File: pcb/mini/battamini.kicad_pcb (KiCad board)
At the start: 2 copper layers, 128.3 x 99.3 mm, 38 parts

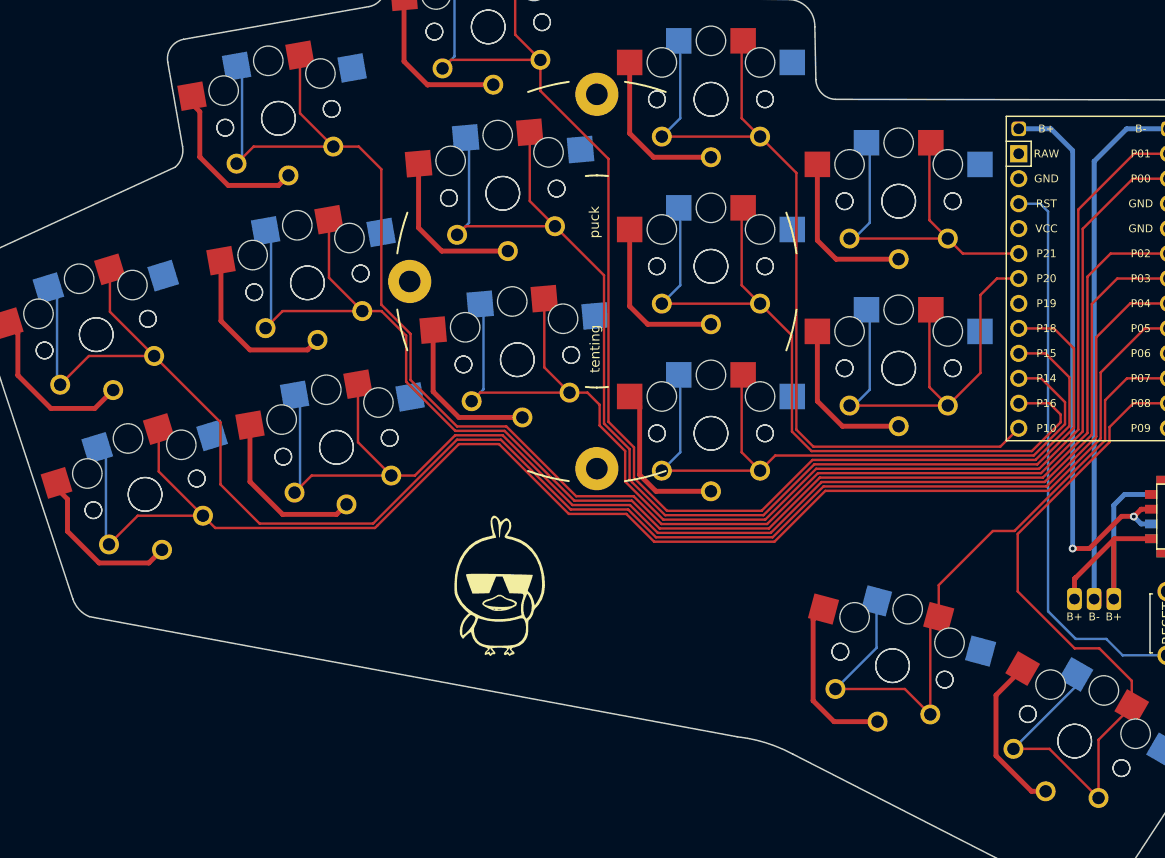
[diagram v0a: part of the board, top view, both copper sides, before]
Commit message: mini routing modification
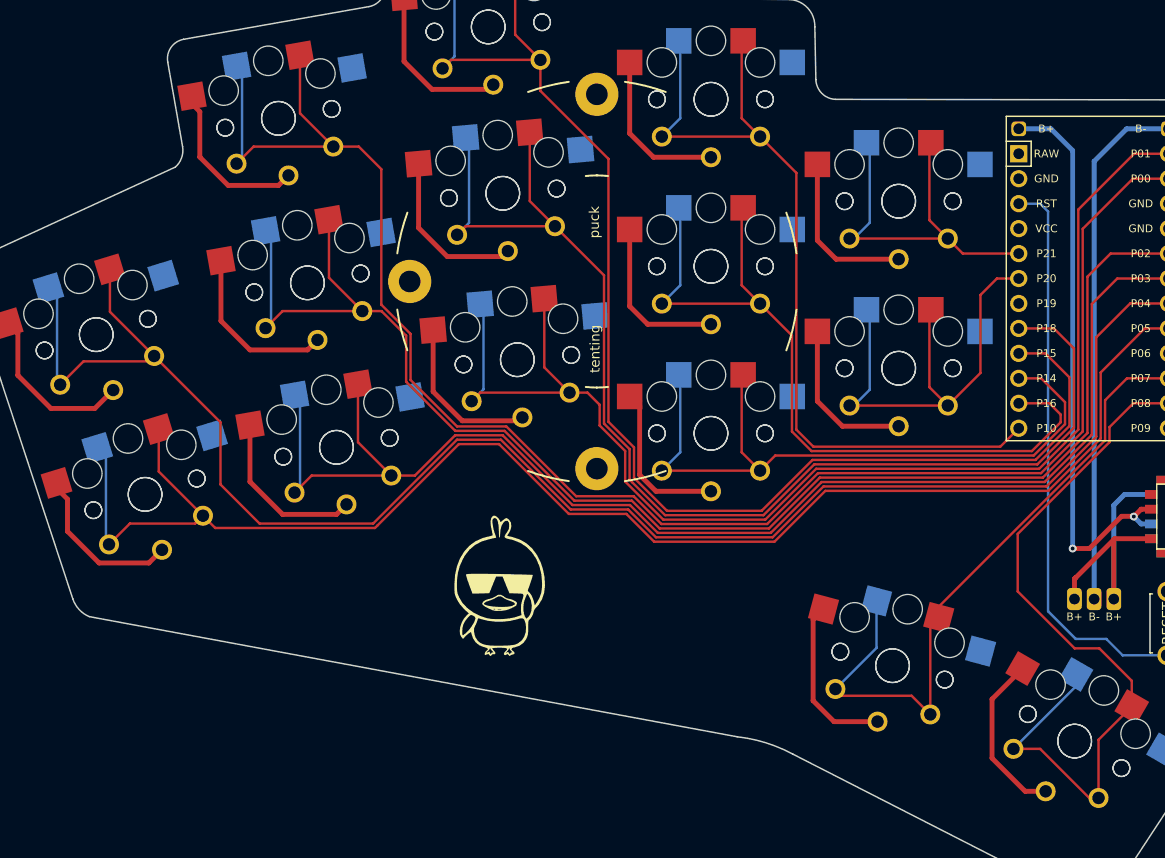
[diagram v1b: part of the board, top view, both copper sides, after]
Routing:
- net GND: track 254.5 -> 256.3 mm
- net P7: track 69.4 -> 68.2 mm

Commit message: updated gerber
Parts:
- removed the REF** at (103.8, -88.1)
- added REF**: Tenting Puck, kbd:Tenting_Puck2, F.Cu at (103.8, -88.1)
